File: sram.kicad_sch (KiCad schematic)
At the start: 25 parts, among them J1 Cache_slot, M1 UM61256AS, M2 UM61256AS, M3 UM61256AS, M4 UM61256AS, M5 UM61256AS, M6 UM61256AS, M7 UM61256AS, M8 UM61256AS, U1 74HCT244, U2 74HCT244

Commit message: 3 errors, 76 warnings
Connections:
- net M5_Q0 is gone; now on net CPU_D0: J1.B56, M5.11 (Q0)
- net M5_Q1 is gone; now on net CPU_D1: J1.B55, M5.12 (Q1)
- net M5_Q2 is gone; now on net CPU_D2: J1.B53, M5.13 (Q2)
- net M5_Q3 is gone; now on net CPU_D3: J1.B52, M5.15 (Q3)
- net M5_Q4 is gone; now on net CPU_D4: J1.B51, M5.16 (Q4)
- net M5_Q5 is gone; now on net CPU_D5: J1.B49, M5.17 (Q5)
- net M5_Q6 is gone; now on net CPU_D6: J1.B48, M5.18 (Q6)
- net M5_Q7 is gone; now on net CPU_D7: J1.B47, M5.19 (Q7)
- net M6_Q0 is gone; now on net CPU_D8: J1.B45, M6.11 (Q0)
- net M6_Q1 is gone; now on net CPU_D9: J1.B44, M6.12 (Q1)
- net M6_Q2 is gone; now on net CPU_D10: J1.B43, M6.13 (Q2)
- net M6_Q3 is gone; now on net CPU_D11: M6.15 (Q3)
- net M6_Q4 is gone; now on net CPU_D12: M6.16 (Q4)
- net M6_Q5 is gone; now on net CPU_D13: M6.17 (Q5)
- net M6_Q6 is gone; now on net CPU_D14: J1.B37, M6.18 (Q6)
- net M6_Q7 is gone; now on net CPU_D15: J1.B36, M6.19 (Q7)
- net M7_Q0 is gone; now on net CPU_D16: M7.11 (Q0)
- net M7_Q1 is gone; now on net CPU_D17: M7.12 (Q1)
- net M7_Q2 is gone; now on net CPU_D18: M7.13 (Q2)
- net M7_Q3 is gone; now on net CPU_D19: M7.15 (Q3)
- net M7_Q4 is gone; now on net CPU_D20: M7.16 (Q4)
- net M7_Q5 is gone; now on net CPU_D21: M7.17 (Q5)
- net M7_Q6 is gone; now on net CPU_D22: M7.18 (Q6)
- net M7_Q7 is gone; now on net CPU_D23: M7.19 (Q7)
- net M8_Q0 is gone; now on net CPU_D24: M8.11 (Q0)
- net M8_Q1 is gone; now on net CPU_D25: M8.12 (Q1)
- net M8_Q2 is gone; now on net CPU_D26: M8.13 (Q2)
- net M8_Q3 is gone; now on net CPU_D27: M8.15 (Q3)
- net M8_Q4 is gone; now on net CPU_D28: M8.16 (Q4)
- net M8_Q5 is gone; now on net CPU_D29: M8.17 (Q5)
- net M8_Q6 is gone; now on net CPU_D30: M8.18 (Q6)
- net M8_Q7 is gone; now on net CPU_D31: M8.19 (Q7)
- net MD1_A9 is gone; now on net CPU_A12: MD1.24 (A9)
- net U2_2A2 is gone; now on net CPU_A14: J1.A49, U2.13 (2A2)
- net a42 is gone; now on net CPU_A9: J1.A42
- net a43 is gone; now on net CPU_A10: J1.A43
- net a45 is gone; now on net CPU_A11: J1.A45
- net a46 is gone; now on net CPU_A12: J1.A46
- net b15 is gone; now on net CPU_D31: J1.B15
- net b16 is gone; now on net CPU_D30: J1.B16
- net b17 is gone; now on net CPU_D29: J1.B17
- net b19 is gone; now on net CPU_D28: J1.B19
- net b20 is gone; now on net CPU_D27: J1.B20
- net b21 is gone; now on net CPU_D26: J1.B21
- net b23 is gone; now on net CPU_D25: J1.B23
- net b24 is gone; now on net CPU_D24: J1.B24
- net b25 is gone; now on net CPU_D23: J1.B25
- net b27 is gone; now on net CPU_D22: J1.B27
- net b28 is gone; now on net CPU_D21: J1.B28
- net b29 is gone; now on net CPU_D20: J1.B29
- net b31 is gone; now on net CPU_D19: J1.B31
- net b39 is gone; now on net CPU_D13: J1.B39
- net b40 is gone; now on net CPU_D12: J1.B40
- net b41 is gone; now on net CPU_D11: J1.B41
- net CPU_A4_SR: now also U2.12 (1Y3)
- net Bank1_CS: now reaches M7.20 (~{CS})
- net Bank1_CS: now also M5.20 (~{CS}), M6.20 (~{CS}), M8.20 (~{CS})
- net Bank1_OE: now reaches M7.22 (~{OE})
- net Bank1_OE: now also M5.22 (~{OE}), M6.22 (~{OE}), M8.22 (~{OE})
- net WE_7: now reaches M7.27 (~{WE})
- net under_U1_3: now reaches J1.A19, J1.A21, J1.A22, J1.A23
- net under_U1_2: now reaches J1.A25, J1.A26, J1.A27, J1.A29
- net Bank0_CS: now reaches M2.20 (~{CS})
- net Bank0_CS: now also M1.20 (~{CS}), M3.20 (~{CS}), M4.20 (~{CS})
- net Bank0_OE: now reaches M2.22 (~{OE})
- net Bank0_OE: now also M1.22 (~{OE}), M3.22 (~{OE}), M4.22 (~{OE})
- net under_tag4: now reaches U1.6 (1A2)
- net CPU_A12: now reaches U2.2 (1A0)
- net CPU_A10: now reaches U2.6 (1A2)
- net CPU_A9: now reaches U2.8 (1A3)
- net under_tag3: now reaches R6.1
- net M1_Q0 renamed CPU_D0
- net M1_Q1 renamed CPU_D1
- net M1_Q2 renamed CPU_D2
- net M1_Q3 renamed CPU_D3
- net M1_Q4 renamed CPU_D4
- net M1_Q5 renamed CPU_D5
- net M1_Q6 renamed CPU_D6
- net M1_Q7 renamed CPU_D7
- net M1_WE# renamed WE_byte0
- net M2_Q0 renamed CPU_D8
- net M2_Q1 renamed CPU_D9
- net M2_Q2 renamed CPU_D10
- net M2_Q3 renamed CPU_D11
- net M2_Q4 renamed CPU_D12
- net M2_Q5 renamed CPU_D13
- net M2_Q6 renamed CPU_D14
- net M2_Q7 renamed CPU_D15
- net M3_Q0 renamed CPU_D16
- net M3_Q1 renamed CPU_D17
- net M3_Q2 renamed CPU_D18
- net M3_Q3 renamed CPU_D19
- net M3_Q4 renamed CPU_D20
- net M3_Q5 renamed CPU_D21
- net M3_Q6 renamed CPU_D22
- net M3_Q7 renamed CPU_D23
- net M4_Q0 renamed CPU_D24
- net M4_Q1 renamed CPU_D25
- net M4_Q2 renamed CPU_D26
- net M4_Q3 renamed CPU_D27
- net M4_Q4 renamed CPU_D28
- net M4_Q5 renamed CPU_D29
- net M4_Q6 renamed CPU_D30
- net M4_Q7 renamed CPU_D31
- net M8_WE# renamed WE_8
- net MD1_A10 renamed CPU_A14
- net MD1_A8 renamed CPU_A11
- net U1_2A0 renamed CPU_A8
- net U1_2A1 renamed CPU_A7
- net U1_2A2 renamed CPU_A6
- net U1_2A3 renamed CPU_A5
- net U2_2A0 renamed CPU_A17
- net U2_2A1 renamed CPU_A15
- net U2_2A3 renamed CPU_A16
- net a1: no longer names the net of J1.A1
- net a10 renamed under_tag6
- net a11 renamed under_tag7
- net a13 renamed under_tag8
- net a15 renamed under_tag9
- net a17 renamed under_tag10
- net a18 renamed under_tag11
- net a2 renamed under_tag12
- net a3 renamed under_tag13
- net a30: no longer names the net of J1.A30
- net a31: no longer names the net of J1.A31
- net a33: no longer names the net of J1.A33
- net a34: no longer names the net of J1.A34
- net a35 renamed under_U1_1
- net a4 renamed under_tag14
- net a51 renamed CPU_A13
- net a54: no longer names the net of J1.A54
- net a55: no longer names the net of J1.A55
- net a6: no longer names the net of J1.A6
- net a7: no longer names the net of J1.A7
- net a8 renamed under_tag5
- no-connect marks 0 -> 9
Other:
- note added: "1OE might be unused hard via to VCC or GND? ----------- 2OE must go to Ground"
- note added: "Bank0: 1 4 7 Bank1: 2 3 5 4 or 8 3 or 7 2 or 6 1 or 5 5 good with 3 or 7"
- note added: "CS: 5 7 8"
- note removed: "1OE might be unused hard via do VCC or GND? ----------- 2OE must go to Ground"
- moved on the sheet: R1, R2, R5, R6, U2

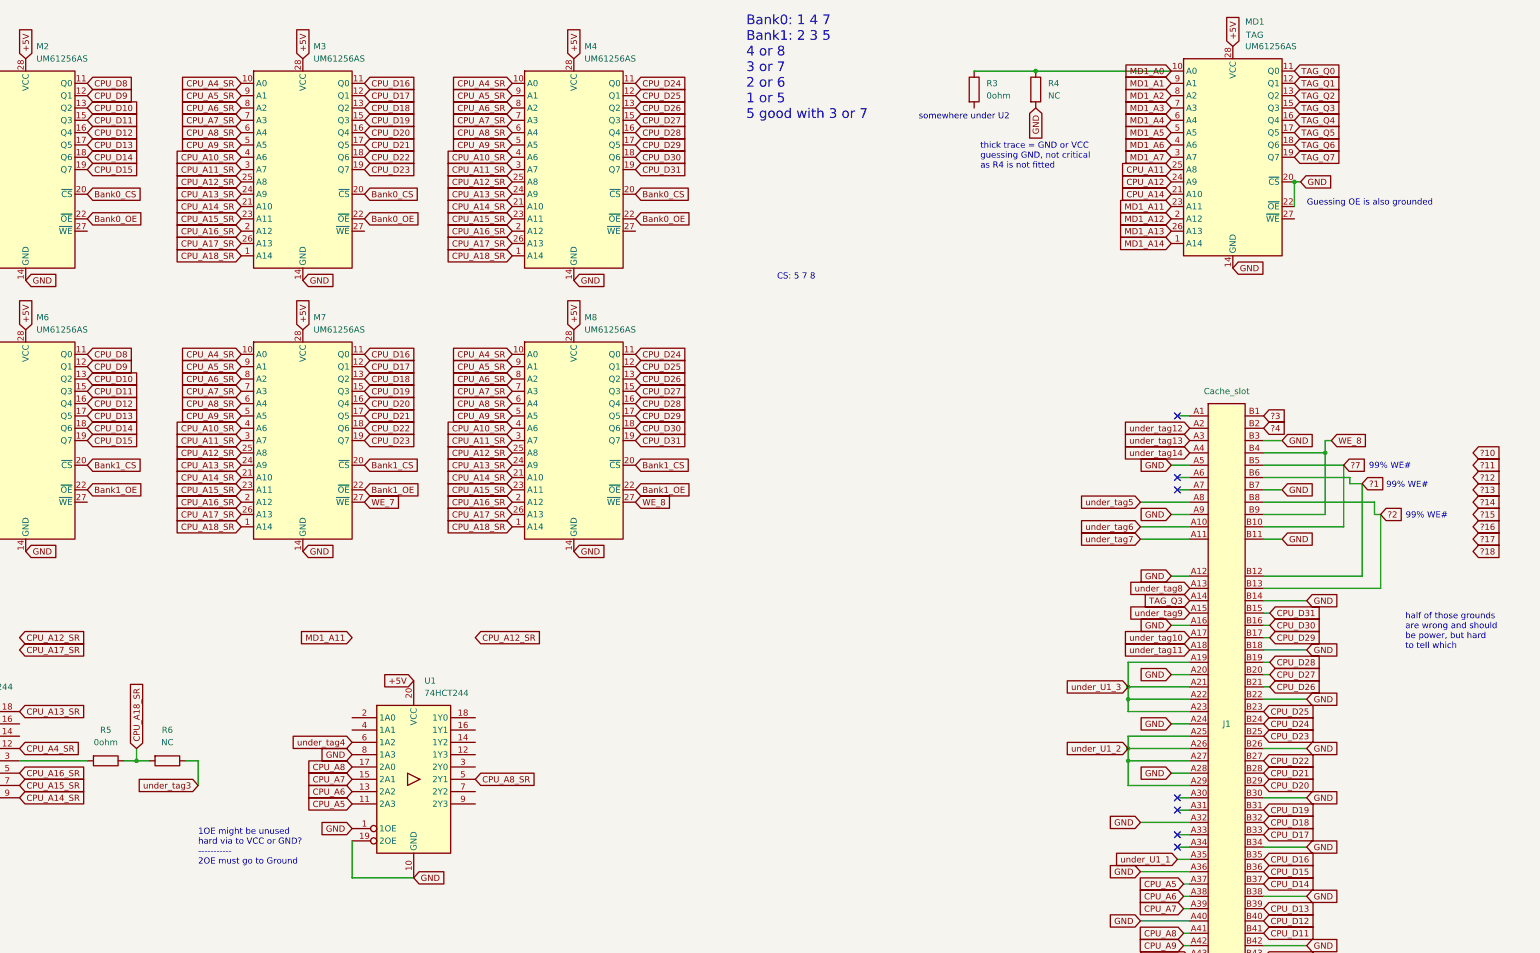
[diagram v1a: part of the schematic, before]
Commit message: 0 drc errors, 62 violations
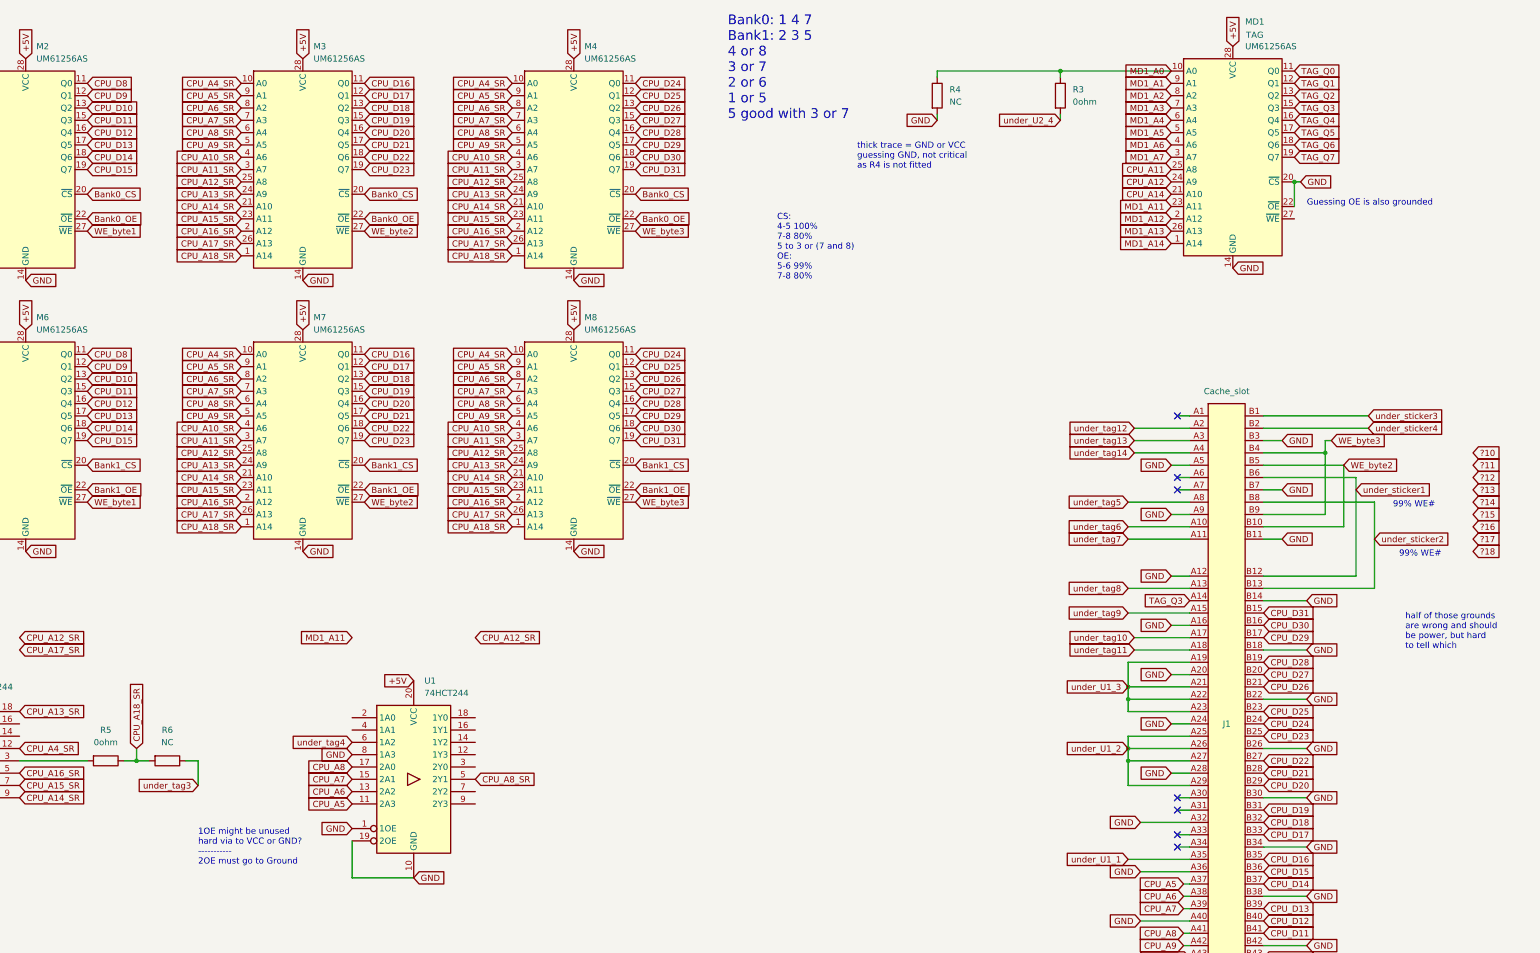
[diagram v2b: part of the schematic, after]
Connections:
- net ?7 is gone; now on net WE_byte2: J1.B10, J1.B5
- net WE_7 is gone; now on net WE_byte2: M7.27 (~{WE})
- net WE_8 is gone; now on net WE_byte3: J1.B4, J1.B9, M8.27 (~{WE})
- net under_U2_4: now reaches R3.2
- net WE_byte1: now reaches M6.27 (~{WE})
- net WE_byte1: now also M2.27 (~{WE})
- net WE_byte3: now reaches M4.27 (~{WE})
- net WE_byte2: now reaches M3.27 (~{WE})
- net ?1 renamed under_sticker1
- net ?2 renamed under_sticker2
- net ?3 renamed under_sticker3
- net ?4 renamed under_sticker4
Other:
- note added: "CS: 4-5 100% 7-8 80% 5 to 3 or (7 and 8) OE: 5-6 99% 7-8 80%"
- note removed: "CS: 5 7 8"
- note removed: "somewhere under U2"
- moved on the sheet: R3, R4

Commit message: 90% there, 0 errors 18 warnings. Just a couple tracks left.
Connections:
- net MD1_A1 is gone; now on net under_U1_1: MD1.9 (A1)
- net MD1_A11 is gone; now on net CPU_A14: MD1.23 (A11)
- net MD1_A12 is gone; now on net CPU_A15: MD1.2 (A12)
- net MD1_A13 is gone; now on net +5V: MD1.26 (A13)
- net MD1_A14 is gone; now on net TAG_A14: MD1.1 (A14)
- net MD1_A2 is gone; now on net CPU_A5: MD1.8 (A2)
- net MD1_A3 is gone; now on net CPU_A6: MD1.7 (A3)
- net MD1_A4 is gone; now on net CPU_A7: MD1.6 (A4)
- net MD1_A5 is gone; now on net CPU_A8: MD1.5 (A5)
- net MD1_A6 is gone; now on net CPU_A9: MD1.4 (A6)
- net MD1_A7 is gone; now on net CPU_A10: MD1.3 (A7)
- net under_U2_4 is gone; now on net CPU_A13: R3.2
- net under_tag10 is gone; now on net TAG_Q1: J1.A17
- net under_tag11 is gone; now on net TAG_Q0: J1.A18
- net under_tag12 is gone; now on net Bank0_CS: J1.A2
- net under_tag13 is gone; now on net Bank0_OE: J1.A3
- net under_tag14 is gone; now on net TAG_WE: J1.A4
- net under_tag4 is gone; now on net TAG_A0: U1.6 (1A2)
- net under_tag5 is gone; now on net TAG_Q7: J1.A8
- net under_tag6 is gone; now on net TAG_Q6: J1.A10
- net under_tag7 is gone; now on net TAG_Q5: J1.A11
- net under_tag8 is gone; now on net TAG_Q4: J1.A13
- net under_tag9 is gone; now on net TAG_Q2: J1.A15
- net +5V: now also J1.B14, J1.B18, J1.B26, J1.B38, J1.B42, J1.B46, J1.B50, J1.B7, R4.2
- net CPU_A14: no longer MD1.21 (A10)
- net CPU_A16: now also MD1.21 (A10)
- net GND: no longer J1.B14, J1.B18, J1.B26, J1.B38, J1.B42, J1.B46, J1.B50, J1.B7, R4.2
- net under_U1_1: now also U1.4 (1A1)
- net TAG_WE: now reaches MD1.27 (~{WE})
- net TAG_A14: now reaches R1.1, R2.2
- net MD1_A0 renamed TAG_A0
- net WE_byte0 renamed Byte_WE0
- net WE_byte1 renamed Byte_WE1
- net WE_byte2 renamed Byte_WE2
- net WE_byte3 renamed Byte_WE3
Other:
- note removed: "Bank0: 1 4 7 Bank1: 2 3 5 4 or 8 3 or 7 2 or 6 1 or 5 5 good with 3 or 7"
- note removed: "CS: 4-5 100% 7-8 80% 5 to 3 or (7 and 8) OE: 5-6 99% 7-8 80%"
- note removed: "Guessing OE is also grounded"
- note removed: "half of those grounds are wrong and should be power, but hard to tell which"
- note removed: "thick trace = GND or VCC guessing GND, not critical as R4 is not fitted"
- note removed: "under TAG ram"
- moved on the sheet: CB1, CB2, CB3, CB4, CT1, CT2, CT3, R4

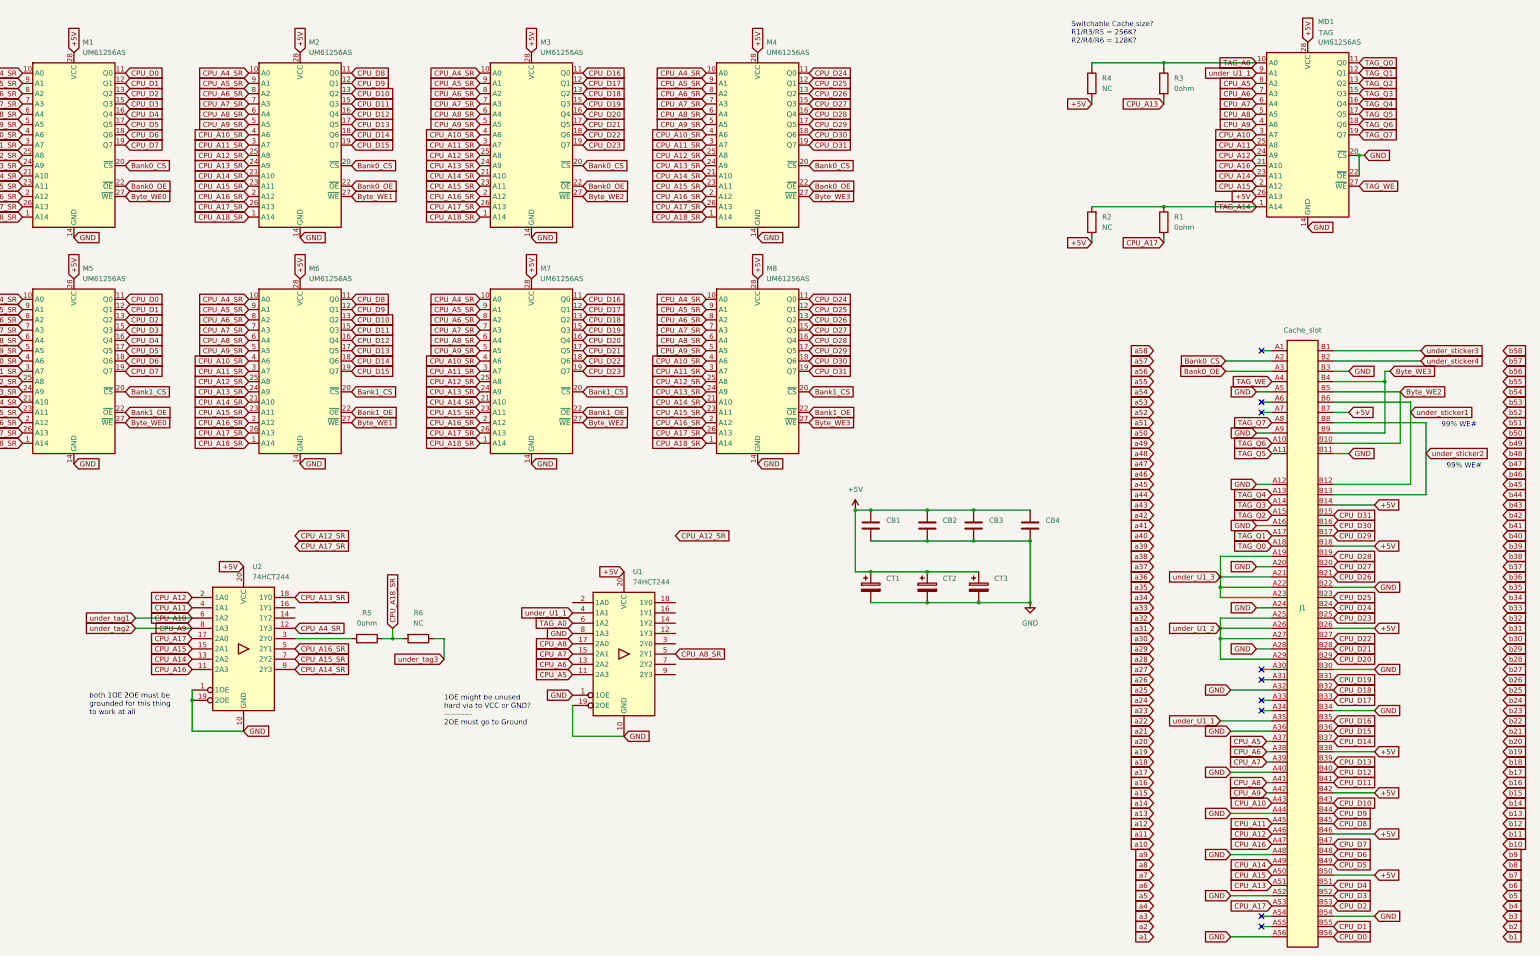
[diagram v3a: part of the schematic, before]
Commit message: 95% there, 0 errors, 7 Warnings. 5 connections missing, 11 guesses and assumptions on U1 U2 and some more on common lines.
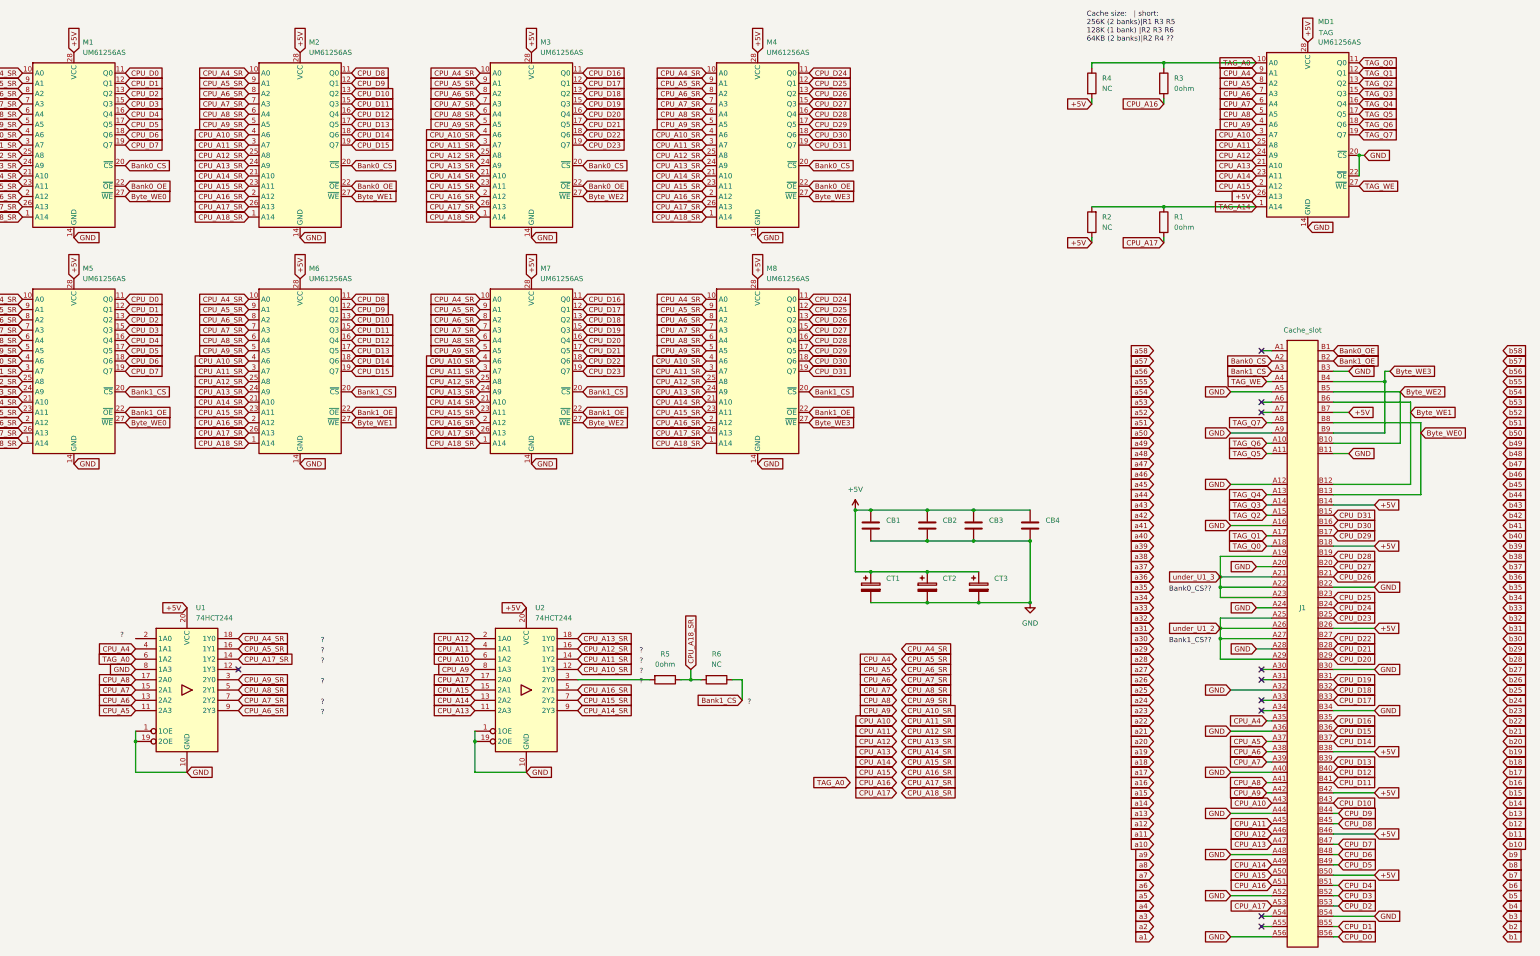
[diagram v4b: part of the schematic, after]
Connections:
- net under_sticker1 is gone; now on net Byte_WE1: J1.B12, J1.B6
- net under_sticker2 is gone; now on net Byte_WE0: J1.B13, J1.B8
- net under_sticker3 is gone; now on net Bank0_OE: J1.B1
- net under_sticker4 is gone; now on net Bank1_OE: J1.B2
- net under_tag3 is gone; now on net Bank1_CS: R6.1
- net Bank0_OE: no longer J1.A3
- net Bank1_CS: now also J1.A3
- net CPU_A10_SR: now also U2.12 (1Y3)
- net CPU_A11_SR: now also U2.14 (1Y2)
- net CPU_A12_SR: now also U2.16 (1Y1)
- net CPU_A13: now also J1.A47, MD1.21 (A10), U2.11 (2A3); no longer J1.A51, R3.2
- net CPU_A16: now also J1.A51, R3.2; no longer J1.A47, MD1.21 (A10), U2.11 (2A3)
- net CPU_A17_SR: now also U1.14 (1Y2)
- net CPU_A4_SR: now also U1.18 (1Y0); no longer U2.12 (1Y3)
- net CPU_A5_SR: now also U1.16 (1Y1)
- net CPU_A6_SR: now also U1.9 (2Y3)
- net CPU_A7_SR: now also U1.7 (2Y2)
- net CPU_A9_SR: now also U1.3 (2Y0)
- net under_U1_1 renamed CPU_A4
- no-connect marks 9 -> 10
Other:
- note added: "?"
- note added: "Bank0_CS??"
- note added: "Bank1_CS??"
- note added: "Cache size: | short: 256K (2 banks)|R1 R3 R5 128K (1 bank) |R2 R3 R6 64KB (2 banks)|R2 R4 ??"
- note removed: "1OE might be unused hard via to VCC or GND? ----------- 2OE must go to Ground"
- note removed: "99% WE#"
- note removed: "Switchable Cache size? R1/R3/R5 = 256K? R2/R4/R6 = 128K?"
- note removed: "both 1OE 2OE must be grounded for this thing to work at all"
- moved on the sheet: R5, R6, U1, U2
